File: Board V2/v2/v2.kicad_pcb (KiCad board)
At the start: 2 copper layers, 69.8 x 71.8 mm, 22 parts, among them J1 Conn_01x06_Male, J2 Screw_Terminal_01x02

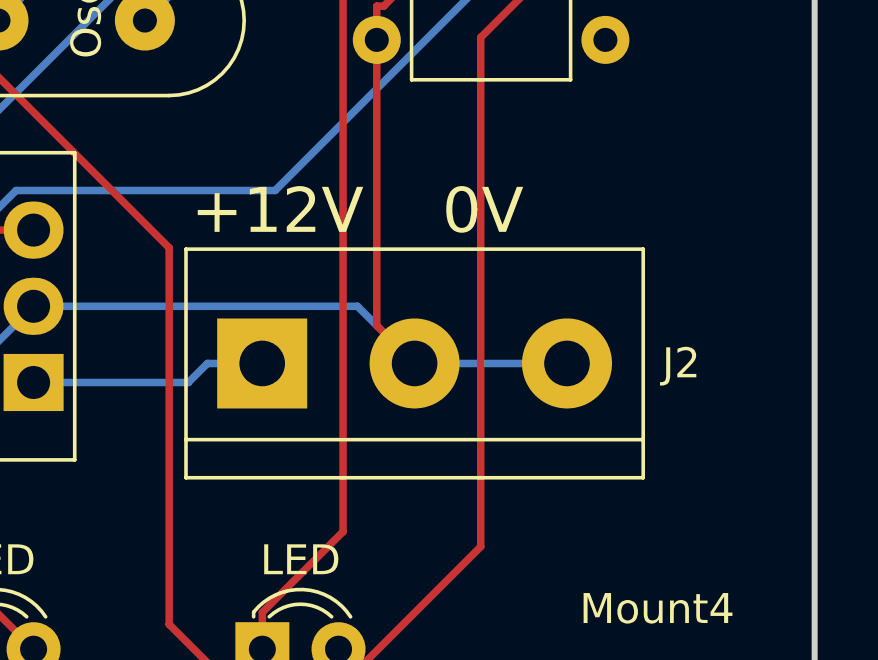
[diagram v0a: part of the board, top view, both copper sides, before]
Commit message: Updated the board with Rikesh's changes
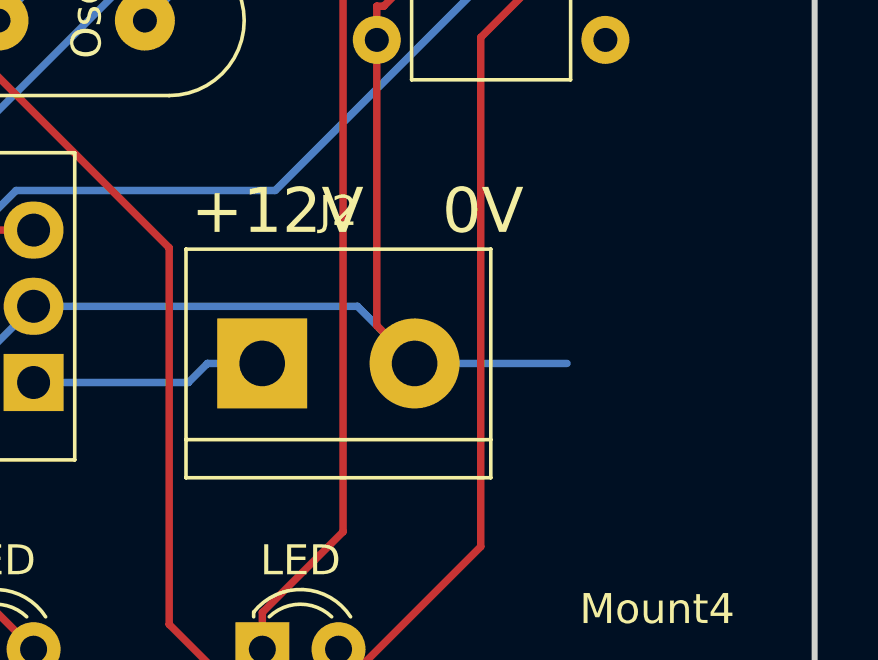
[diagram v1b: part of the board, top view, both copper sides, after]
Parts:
- J2: footprint TerminalBlock:TerminalBlock_bornier-3_P5.08mm -> TerminalBlock:TerminalBlock_bornier-2_P5.08mm
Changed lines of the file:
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@@
     (pad "1" thru_hole circle (at 0 0) (size 5 5) (drill 3.5) (layers F&B.Cu *.Mask))
   )
-  (footprint "TerminalBlock:TerminalBlock_bornier-3_P5.08mm" (layer "F.Cu")
+  (footprint "TerminalBlock:TerminalBlock_bornier-2_P5.08mm" (layer "F.Cu")
     (at 76.835 67.31)
-    (descr "simple 3-pin terminal block, pitch 5.08mm, revamped version of bornier3")
-    (tags "terminal block bornier3")
+    (descr "simple 2-pin terminal block, pitch 5.08mm, revamped version of bornier2")
+    (tags "terminal block bornier2")
     (property "Sheetfile" "v2.kicad_sch")
     (property "Sheetname" "")
     (attr through_hole)
-    (fp_text reference "J2" (at 13.97 0) (layer "F.SilkS")
+    (fp_text reference "J2" (at 2.54 -5.08) (layer "F.SilkS")
       (effects (font (size 1 1) (thickness 0.15)))
     )
-    (fp_text value "Screw_Terminal_01x02" (at 5.08 5.08) (layer "F.Fab")
+    (fp_text value "Screw_Terminal_01x02" (at 2.54 5.08) (layer "F.Fab")
       (effects (font (size 1 1) (thickness 0.15)))
     )
-    (fp_text user "${REFERENCE}" (at 5.08 0) (layer "F.Fab")
+    (fp_text user "${REFERENCE}" (at 2.54 0) (layer "F.Fab")
       (effects (font (size 1 1) (thickness 0.15)))
     )
-    (fp_line (start -2.54 3.81) (end 12.7 3.81) (layer "F.SilkS") (width 0.12))
-    (fp_line (start -2.54 3.81) (end -2.54 -3.81) (layer "F.SilkS") (width 0.12))
-    (fp_line (start -2.54 2.54) (end 12.7 2.54) (layer "F.SilkS") (width 0.12))
-    (fp_line (start 12.7 3.81) (end 12.7 -3.81) (layer "F.SilkS") (width 0.12))
-    (fp_line (start -2.54 -3.81) (end 12.7 -3.81) (layer "F.SilkS") (width 0.12))
-    (fp_line (start -2.72 -4) (end -2.72 4) (layer "F.CrtYd") (width 0.05))
-    (fp_line (start -2.72 -4) (end 12.88 -4) (layer "F.CrtYd") (width 0.05))
-    (fp_line (start 12.88 4) (end -2.72 4) (layer "F.CrtYd") (width 0.05))
-    (fp_line (start 12.88 4) (end 12.88 -4) (layer "F.CrtYd") (width 0.05))
-    (fp_line (start -2.47 3.75) (end -2.47 -3.75) (layer "F.Fab") (width 0.1))
-    (fp_line (start -2.47 -3.75) (end 12.63 -3.75) (layer "F.Fab") (width 0.1))
-    (fp_line (start 12.63 -3.75) (end 12.63 3.75) (layer "F.Fab") (width 0.1))
-    (fp_line (start 12.63 3.75) (end -2.47 3.75) (layer "F.Fab") (width 0.1))
-    (fp_line (start -2.47 2.55) (end 12.63 2.55) (layer "F.Fab") (width 0.1))
+    (fp_line (start 7.62 -3.81) (end -2.54 -3.81) (layer "F.SilkS") (width 0.12))
+    (fp_line (start 7.62 3.81) (end 7.62 -3.81) (layer "F.SilkS") (width 0.12))
+    (fp_line (start -2.54 3.81) (end 7.62 3.81) (layer "F.SilkS") (width 0.12))
+    (fp_line (start 7.62 2.54) (end -2.54 2.54) (layer "F.SilkS") (width 0.12))
+    (fp_line (start -2.54 -3.81) (end -2.54 3.81) (layer "F.SilkS") (width 0.12))
+    (fp_line (start 7.79 4) (end -2.71 4) (layer "F.CrtYd") (width 0.05))
+    (fp_line (start 7.79 4) (end 7.79 -4) (layer "F.CrtYd") (width 0.05))
+    (fp_line (start -2.71 -4) (end 7.79 -4) (layer "F.CrtYd") (width 0.05))
+    (fp_line (start -2.71 -4) (end -2.71 4) (layer "F.CrtYd") (width 0.05))
+    (fp_line (start 7.54 3.75) (end 7.54 -3.75) (layer "F.Fab") (width 0.1))
+    (fp_line (start -2.41 2.55) (end 7.49 2.55) (layer "F.Fab") (width 0.1))
+    (fp_line (start -2.46 -3.75) (end -2.46 3.75) (layer "F.Fab") (width 0.1))
+    (fp_line (start -2.46 3.75) (end 7.54 3.75) (layer "F.Fab") (width 0.1))
+    (fp_line (start 7.54 -3.75) (end -2.46 -3.75) (layer "F.Fab") (width 0.1))
     (pad "1" thru_hole rect (at 0 0) (size 3 3) (drill 1.52) (layers *.Cu *.Mask)
       (net 47 "V_IN") (pinfunction "Pin_1") (pintype "passive"))
     (pad "2" thru_hole circle (at 5.08 0) (size 3 3) (drill 1.52) (layers *.Cu *.Mask)
       (net 4 "GND") (pinfunction "Pin_2") (pintype "passive"))
-    (pad "3" thru_hole circle (at 10.16 0) (size 3 3) (drill 1.52) (layers *.Cu *.Mask))
-    (model "${KICAD6_3DMODEL_DIR}/TerminalBlock.3dshapes/TerminalBlock_bornier-3_P5.08mm.wrl"
-      (offset (xyz 5.079999924 0 0))
+    (model "${KICAD6_3DMODEL_DIR}/TerminalBlock.3dshapes/TerminalBlock_bornier-2_P5.08mm.wrl"
+      (offset (xyz 2.539999962 0 0))
       (scale (xyz 1 1 1))
       (rotate (xyz 0 0 0))
